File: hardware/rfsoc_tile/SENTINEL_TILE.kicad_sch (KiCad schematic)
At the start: 118 parts, among them J1 SOM CONN A, J10 RX1, J11 RX2, J12 RX3, J13 RX4, J14 RX5, J15 RX6, J16 RX7, J17 RX8, J18 RXCAL, J2 SOM CONN B, J20 TX1, J21 TX2, J22 TX3, J23 TX4, J24 TX5, J25 TX6, J26 TX7, J27 TX8, J28 TXCAL, J3 BACKPLANE, J4 CLOCK, J5 CAL CTRL, J6 PSU LINK, J7 QSFP28, J8 12V IN, T1 1:2, T11 1:2, T12 1:2, T13 1:2, T14 1:2, T15 1:2, T16 1:2, T17 1:2, T18 1:2, T19 1:2, T2 1:2, T3 1:2, T4 1:2, T5 1:2, T6 1:2, T7 1:2, T8 1:2, T9 1:2, U1 THVD1450, U10 LMR33630, U2 THVD1450, U3 THVD1450, U4 THVD1450, U5 THVD1450, U6 THVD1450, U7 THVD1450, U8 THVD1450, U9 THVD1450

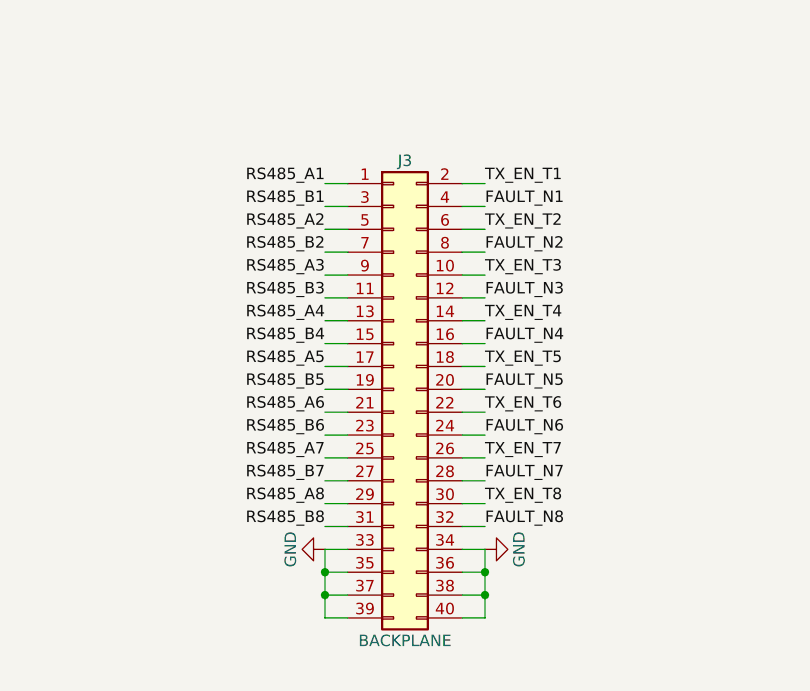
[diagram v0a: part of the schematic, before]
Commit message: Five boards DRC-clean, BOMs, layout engine improvements
- Backplane, clock & timing, calibration network, PSU and feed board layouts now pass
  KiCad DRC with zero errors and zero unconnected items
- T/R module: 0 DRC errors, 6 connections left to route by hand
- Calibration selector redesigned as an SPDT tree (replaces the fine-pitch SP8T)
- PSU: IPC-2221 2.5 mm high-voltage clearance via KiCad custom rules
- Backplane/tile cable re-pinned (slots 1-4 left column, 5-8 right) for routability
- Grouped BOM CSV for every board (hardware/tools/export_bom.sh)
- Router: partial routing, neck-downs at fine-pitch pins, long-axis fan-out,
  NPTH obstacles, pour-net connectivity, domain-aware clearance, rip-up tuning

Co-Authored-By: Claude Opus 5.5 <noreply@anthropic.com>
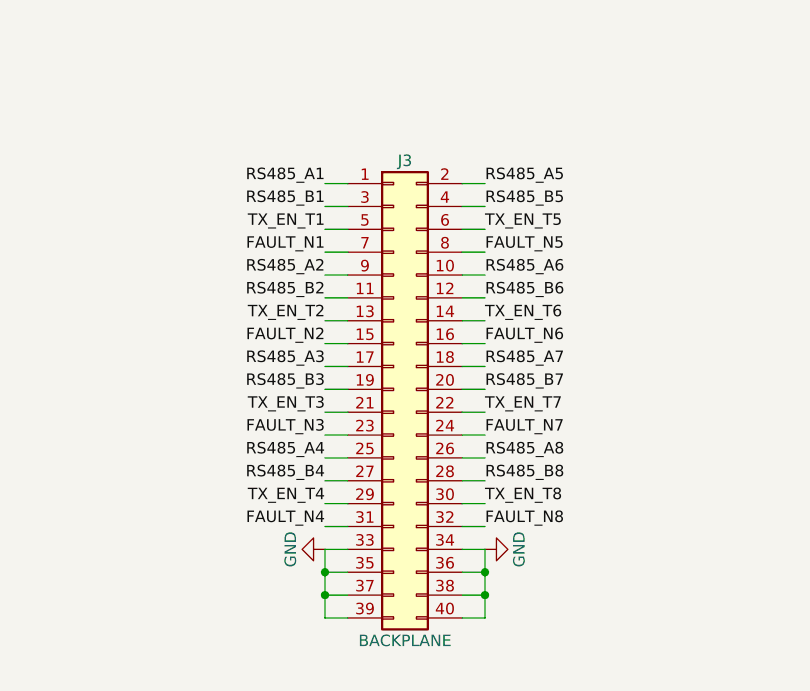
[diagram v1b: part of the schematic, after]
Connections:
- net FAULT_N1: now also J3.7 (Pin_7); no longer J3.4 (Pin_4)
- net FAULT_N2: now also J3.15 (Pin_15); no longer J3.8 (Pin_8)
- net FAULT_N3: now also J3.23 (Pin_23); no longer J3.12 (Pin_12)
- net FAULT_N4: now also J3.31 (Pin_31); no longer J3.16 (Pin_16)
- net FAULT_N5: now also J3.8 (Pin_8); no longer J3.20 (Pin_20)
- net FAULT_N6: now also J3.16 (Pin_16); no longer J3.24 (Pin_24)
- net FAULT_N7: now also J3.24 (Pin_24); no longer J3.28 (Pin_28)
- net RS485_A2: now also J3.9 (Pin_9); no longer J3.5 (Pin_5)
- net RS485_A3: now also J3.17 (Pin_17); no longer J3.9 (Pin_9)
- net RS485_A4: now also J3.25 (Pin_25); no longer J3.13 (Pin_13)
- net RS485_A5: now also J3.2 (Pin_2); no longer J3.17 (Pin_17)
- net RS485_A6: now also J3.10 (Pin_10); no longer J3.21 (Pin_21)
- net RS485_A7: now also J3.18 (Pin_18); no longer J3.25 (Pin_25)
- net RS485_A8: now also J3.26 (Pin_26); no longer J3.29 (Pin_29)
- net RS485_B2: now also J3.11 (Pin_11); no longer J3.7 (Pin_7)
- net RS485_B3: now also J3.19 (Pin_19); no longer J3.11 (Pin_11)
- net RS485_B4: now also J3.27 (Pin_27); no longer J3.15 (Pin_15)
- net RS485_B5: now also J3.4 (Pin_4); no longer J3.19 (Pin_19)
- net RS485_B6: now also J3.12 (Pin_12); no longer J3.23 (Pin_23)
- net RS485_B7: now also J3.20 (Pin_20); no longer J3.27 (Pin_27)
- net RS485_B8: now also J3.28 (Pin_28); no longer J3.31 (Pin_31)
- net TX_EN_T1: now also J3.5 (Pin_5); no longer J3.2 (Pin_2)
- net TX_EN_T2: now also J3.13 (Pin_13); no longer J3.6 (Pin_6)
- net TX_EN_T3: now also J3.21 (Pin_21); no longer J3.10 (Pin_10)
- net TX_EN_T4: now also J3.29 (Pin_29); no longer J3.14 (Pin_14)
- net TX_EN_T5: now also J3.6 (Pin_6); no longer J3.18 (Pin_18)
- net TX_EN_T6: now also J3.14 (Pin_14); no longer J3.22 (Pin_22)
- net TX_EN_T7: now also J3.22 (Pin_22); no longer J3.26 (Pin_26)
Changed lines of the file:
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@@
 		)
 	)
-	(label "TX_EN_T1"
+	(label "RS485_A5"
 		(at 441.96 358.14 0)
 		(fields_autoplaced yes)
@@
 		)
 	)
+	(label "RS485_B5"
+		(at 441.96 360.68 0)
+		(fields_autoplaced yes)
+		(effects
+			(font
+				(size 1.27 1.27)
+			)
+			(justify left bottom)
+		)
+	)
+	(label "TX_EN_T1"
+		(at 424.18 363.22 180)
+		(fields_autoplaced yes)
+		(effects
+			(font
+				(size 1.27 1.27)
+			)
+			(justify right bottom)
+		)
+	)
+	(label "TX_EN_T5"
+		(at 441.96 363.22 0)
+		(fields_autoplaced yes)
+		(effects
+			(font
+				(size 1.27 1.27)
+			)
+			(justify left bottom)
+		)
+	)
 	(label "FAULT_N1"
-		(at 441.96 360.68 0)
+		(at 424.18 365.76 180)
+		(fields_autoplaced yes)
+		(effects
+			(font
+				(size 1.27 1.27)
+			)
+			(justify right bottom)
+		)
+	)
+	(label "FAULT_N5"
+		(at 441.96 365.76 0)
 		(fields_autoplaced yes)
 		(effects
@@
 	)
 	(label "RS485_A2"
-		(at 424.18 363.22 180)
-		(fields_autoplaced yes)
-		(effects
-			(font
-				(size 1.27 1.27)
-			)
-			(justify right bottom)
+		(at 424.18 368.3 180)
+		(fields_autoplaced yes)
+		(effects
+			(font
+				(size 1.27 1.27)
+			)
+			(justify right bottom)
+		)
+	)
+	(label "RS485_A6"
+		(at 441.96 368.3 0)
+		(fields_autoplaced yes)
+		(effects
+			(font
+				(size 1.27 1.27)
+			)
+			(justify left bottom)
+		)
+	)
+	(label "RS485_B2"
+		(at 424.18 370.84 180)
+		(fields_autoplaced yes)
+		(effects
+			(font
+				(size 1.27 1.27)
+			)
+			(justify right bottom)
+		)
+	)
+	(label "RS485_B6"
+		(at 441.96 370.84 0)
+		(fields_autoplaced yes)
+		(effects
+			(font
+				(size 1.27 1.27)
+			)
+			(justify left bottom)
 		)
 	)
 	(label "TX_EN_T2"
-		(at 441.96 363.22 0)
-		(fields_autoplaced yes)
-		(effects
-			(font
-				(size 1.27 1.27)
-			)
-			(justify left bottom)
-		)
-	)
-	(label "RS485_B2"
-		(at 424.18 365.76 180)
-		(fields_autoplaced yes)
-		(effects
-			(font
-				(size 1.27 1.27)
-			)
-			(justify right bottom)
+		(at 424.18 373.38 180)
+		(fields_autoplaced yes)
+		(effects
+			(font
+				(size 1.27 1.27)
+			)
+			(justify right bottom)
+		)
+	)
+	(label "TX_EN_T6"
+		(at 441.96 373.38 0)
+		(fields_autoplaced yes)
+		(effects
+			(font
+				(size 1.27 1.27)
+			)
+			(justify left bottom)
 		)
 	)
 	(label "FAULT_N2"
-		(at 441.96 365.76 0)
+		(at 424.18 375.92 180)
+		(fields_autoplaced yes)
+		(effects
+			(font
+				(size 1.27 1.27)
+			)
+			(justify right bottom)
+		)
+	)
+	(label "FAULT_N6"
+		(at 441.96 375.92 0)
 		(fields_autoplaced yes)
 		(effects
@@
 	)
 	(label "RS485_A3"
-		(at 424.18 368.3 180)
-		(fields_autoplaced yes)
-		(effects
-			(font
-				(size 1.27 1.27)
-			)
-			(justify right bottom)
+		(at 424.18 378.46 180)
+		(fields_autoplaced yes)
+		(effects
+			(font
+				(size 1.27 1.27)
+			)
+			(justify right bottom)
+		)
+	)
+	(label "RS485_A7"
+		(at 441.96 378.46 0)
+		(fields_autoplaced yes)
+		(effects
+			(font
+				(size 1.27 1.27)
+			)
+			(justify left bottom)
+		)
+	)
+	(label "RS485_B3"
+		(at 424.18 381 180)
+		(fields_autoplaced yes)
+		(effects
+			(font
+				(size 1.27 1.27)
+			)
+			(justify right bottom)
+		)
+	)
+	(label "RS485_B7"
+		(at 441.96 381 0)
+		(fields_autoplaced yes)
+		(effects
+			(font
+				(size 1.27 1.27)
+			)
+			(justify left bottom)
 		)
 	)
 	(label "TX_EN_T3"
-		(at 441.96 368.3 0)
-		(fields_autoplaced yes)
-		(effects
-			(font
-				(size 1.27 1.27)
-			)
-			(justify left bottom)
-		)
-	)
-	(label "RS485_B3"
-		(at 424.18 370.84 180)
-		(fields_autoplaced yes)
-		(effects
-			(font
-				(size 1.27 1.27)
-			)
-			(justify right bottom)
+		(at 424.18 383.54 180)
+		(fields_autoplaced yes)
+		(effects
+			(font
+				(size 1.27 1.27)
+			)
+			(justify right bottom)
+		)
+	)
+	(label "TX_EN_T7"
+		(at 441.96 383.54 0)
+		(fields_autoplaced yes)
+		(effects
+			(font
+				(size 1.27 1.27)
+			)
+			(justify left bottom)
 		)
 	)
 	(label "FAULT_N3"
-		(at 441.96 370.84 0)
+		(at 424.18 386.08 180)
+		(fields_autoplaced yes)
+		(effects
+			(font
+				(size 1.27 1.27)
+			)
+			(justify right bottom)
+		)
+	)
+	(label "FAULT_N7"
+		(at 441.96 386.08 0)
 		(fields_autoplaced yes)
 		(effects
@@
 	)
 	(label "RS485_A4"
-		(at 424.18 373.38 180)
-		(fields_autoplaced yes)
-		(effects
-			(font
-				(size 1.27 1.27)
-			)
-			(justify right bottom)
+		(at 424.18 388.62 180)
+		(fields_autoplaced yes)
+		(effects
+			(font
+				(size 1.27 1.27)
+			)
+			(justify right bottom)
+		)
+	)
+	(label "RS485_A8"
+		(at 441.96 388.62 0)
+		(fields_autoplaced yes)
+		(effects
+			(font
+				(size 1.27 1.27)
+			)
+			(justify left bottom)
+		)
+	)
+	(label "RS485_B4"
+		(at 424.18 391.16 180)
+		(fields_autoplaced yes)
+		(effects
+			(font
+				(size 1.27 1.27)
+			)
+			(justify right bottom)
+		)
+	)
+	(label "RS485_B8"
+		(at 441.96 391.16 0)
+		(fields_autoplaced yes)
+		(effects
+			(font
+				(size 1.27 1.27)
+			)
+			(justify left bottom)
 		)
 	)
 	(label "TX_EN_T4"
-		(at 441.96 373.38 0)
-		(fields_autoplaced yes)
-		(effects
-			(font
-				(size 1.27 1.27)
-			)
-			(justify left bottom)
-		)
-	)
-	(label "RS485_B4"
-		(at 424.18 375.92 180)
-		(fields_autoplaced yes)
-		(effects
-			(font
-				(size 1.27 1.27)
-			)
-			(justify right bottom)
-		)
-	)
-	(label "FAULT_N4"
-		(at 441.96 375.92 0)
-		(fields_autoplaced yes)
-		(effects
-			(font
-				(size 1.27 1.27)
-			)
-			(justify left bottom)
-		)
-	)
-	(label "RS485_A5"
-		(at 424.18 378.46 180)
-		(fields_autoplaced yes)
-		(effects
-			(font
-				(size 1.27 1.27)
-			)
-			(justify right bottom)
-		)
-	)
-	(label "TX_EN_T5"
-		(at 441.96 378.46 0)
-		(fields_autoplaced yes)
-		(effects
-			(font
-				(size 1.27 1.27)
-			)
-			(justify left bottom)
-		)
-	)
-	(label "RS485_B5"
-		(at 424.18 381 180)
-		(fields_autoplaced yes)
-		(effects
-			(font
-				(size 1.27 1.27)
-			)
-			(justify right bottom)
-		)
-	)
-	(label "FAULT_N5"
-		(at 441.96 381 0)
-		(fields_autoplaced yes)
-		(effects
-			(font
-				(size 1.27 1.27)
-			)
-			(justify left bottom)
-		)
-	)
-	(label "RS485_A6"
-		(at 424.18 383.54 180)
-		(fields_autoplaced yes)
-		(effects
-			(font
-				(size 1.27 1.27)
-			)
-			(justify right bottom)
-		)
-	)
-	(label "TX_EN_T6"
-		(at 441.96 383.54 0)
-		(fields_autoplaced yes)
-		(effects
-			(font
-				(size 1.27 1.27)
-			)
-			(justify left bottom)
-		)
-	)
-	(label "RS485_B6"
-		(at 424.18 386.08 180)
-		(fields_autoplaced yes)
-		(effects
-			(font
-				(size 1.27 1.27)
-			)
-			(justify right bottom)
-		)
-	)
-	(label "FAULT_N6"
-		(at 441.96 386.08 0)
-		(fields_autoplaced yes)
-		(effects
-			(font
-				(size 1.27 1.27)
-			)
-			(justify left bottom)
-		)
-	)
-	(label "RS485_A7"
-		(at 424.18 388.62 180)
-		(fields_autoplaced yes)
-		(effects
-			(font
-				(size 1.27 1.27)
-			)
-			(justify right bottom)
-		)
-	)
-	(label "TX_EN_T7"
-		(at 441.96 388.62 0)
-		(fields_autoplaced yes)
-		(effects
-			(font
-				(size 1.27 1.27)
-			)
-			(justify left bottom)
-		)
-	)
-	(label "RS485_B7"
-		(at 424.18 391.16 180)
-		(fields_autoplaced yes)
-		(effects
-			(font
-				(size 1.27 1.27)
-			)
-			(justify right bottom)
-		)
-	)
-	(label "FAULT_N7"
-		(at 441.96 391.16 0)
-		(fields_autoplaced yes)
-		(effects
-			(font
-				(size 1.27 1.27)
-			)
-			(justify left bottom)
-		)
-	)
-	(label "RS485_A8"
 		(at 424.18 393.7 180)
 		(fields_autoplaced yes)
@@
 		)
 	)
-	(label "RS485_B8"
+	(label "FAULT_N4"
 		(at 424.18 396.24 180)
 		(fields_autoplaced yes)

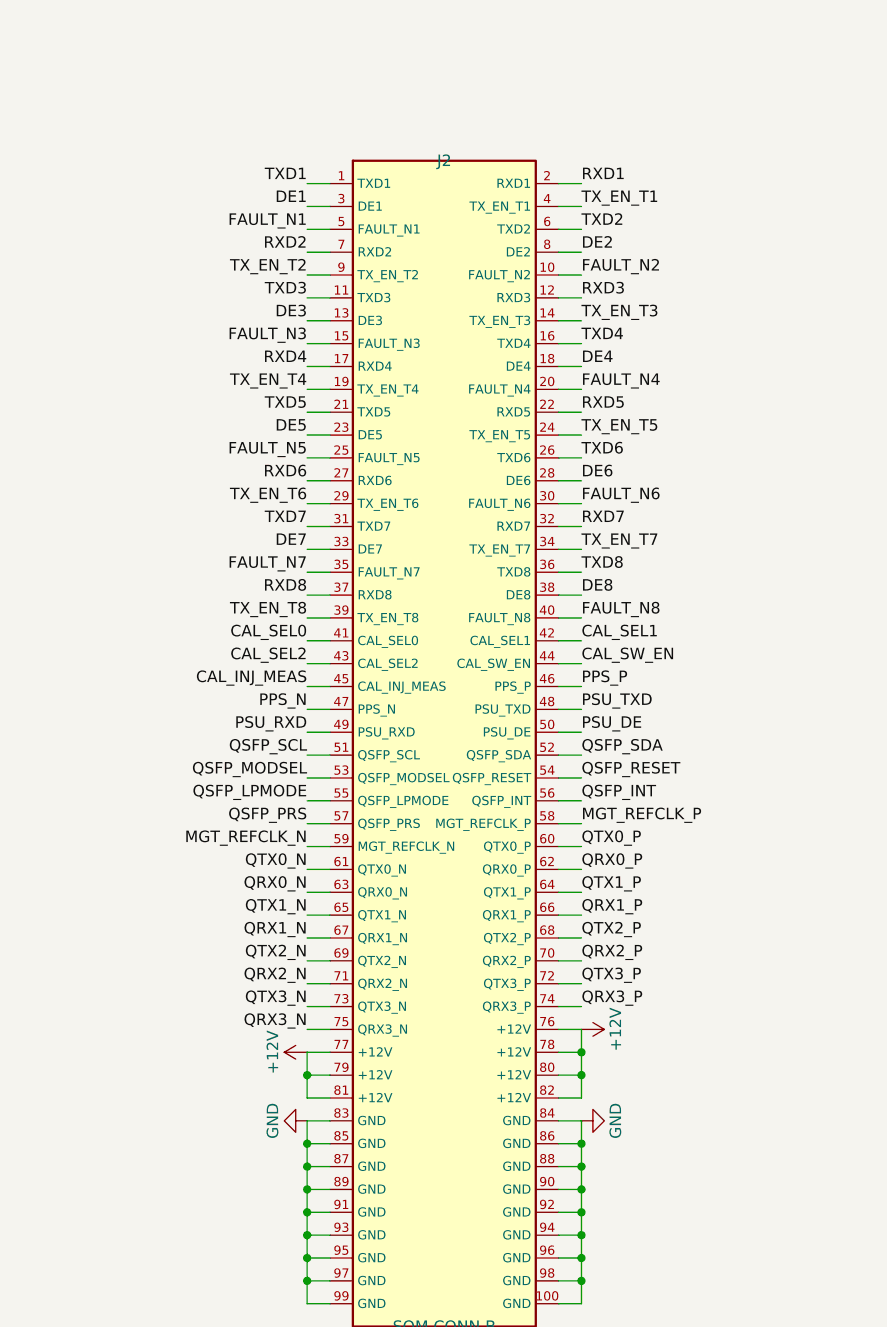
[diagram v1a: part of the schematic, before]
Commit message: RFSoC tile: 320 x 260 mm, routed with EasyEDA Pro, DRC clean
- Board enlarged from 240 x 190 to 320 x 260 mm; SOM connector B pins
  grouped by row toward their destinations (RS-485 / control side).
- Routing done by the EasyEDA Pro autorouter (Top / In2 / Bottom, In1 kept
  as solid GND) and imported back into KiCad: 0 DRC errors, 0 unrouted.
- tools/import_easyeda.py replays easyeda_routes.json onto the KiCad board;
  tools/layer_preview.py draws copper previews from any finished board.
- Regenerated gerbers, 3D view, BOM, figures, report and README (6 of 7
  layouts now DRC clean).

Co-Authored-By: Claude Opus 5.5 <noreply@anthropic.com>
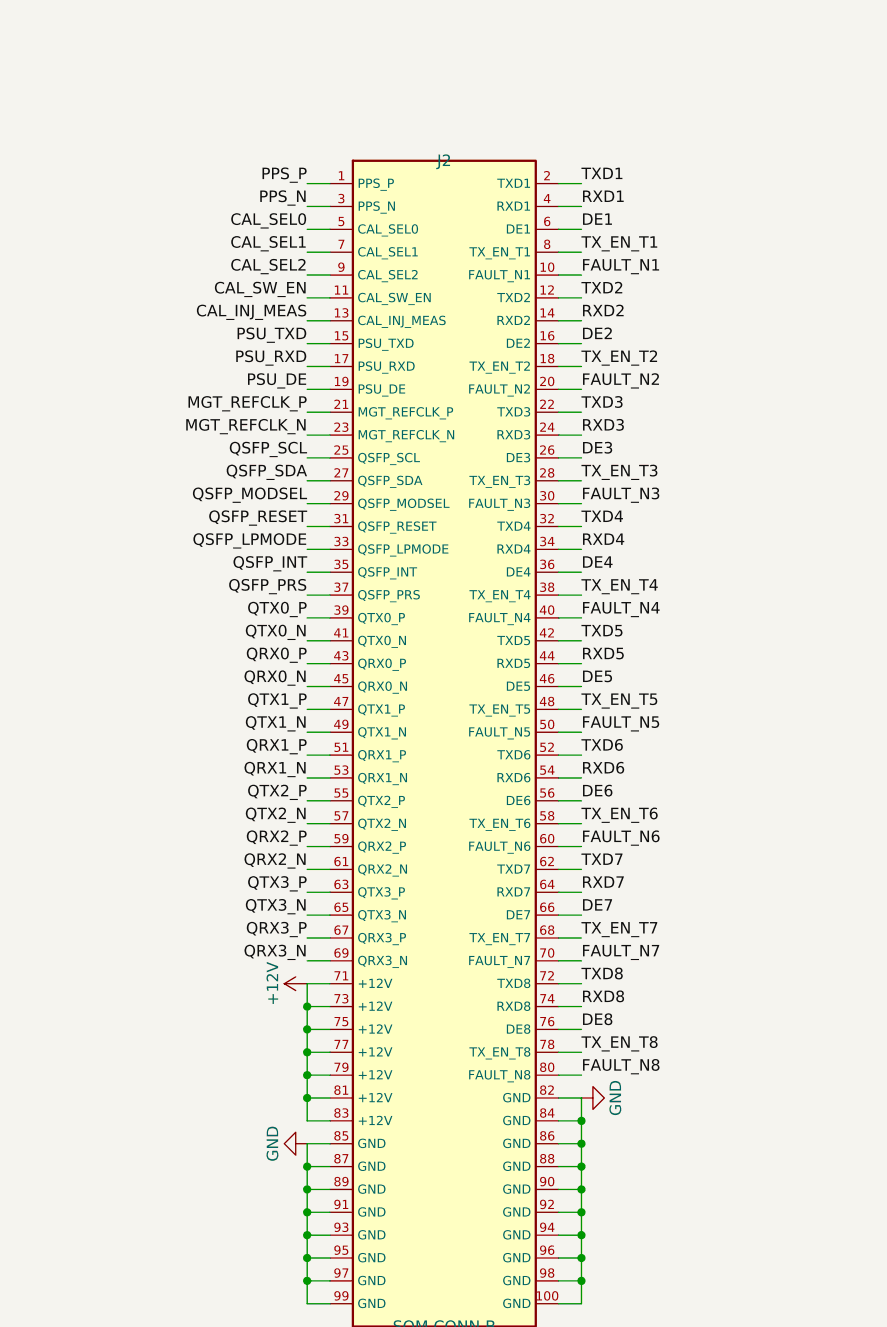
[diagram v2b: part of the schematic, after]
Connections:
- net +12V: now also J2.71 (+12V), J2.73 (+12V), J2.75 (+12V), J2.83 (+12V); no longer J2.76 (+12V), J2.78 (+12V), J2.80 (+12V), J2.82 (+12V)
- net CAL_INJ_MEAS: now also J2.13 (CAL_INJ_MEAS); no longer J2.45 (CAL_INJ_MEAS)
- net CAL_SEL0: now also J2.5 (CAL_SEL0); no longer J2.41 (CAL_SEL0)
- net CAL_SEL1: now also J2.7 (CAL_SEL1); no longer J2.42 (CAL_SEL1)
- net CAL_SEL2: now also J2.9 (CAL_SEL2); no longer J2.43 (CAL_SEL2)
- net CAL_SW_EN: now also J2.11 (CAL_SW_EN); no longer J2.44 (CAL_SW_EN)
- net DE1: now also J2.6 (DE1); no longer J2.3 (DE1)
- net DE2: now also J2.16 (DE2); no longer J2.8 (DE2)
- net DE3: now also J2.26 (DE3); no longer J2.13 (DE3)
- net DE4: now also J2.36 (DE4); no longer J2.18 (DE4)
- net DE5: now also J2.46 (DE5); no longer J2.23 (DE5)
- net DE6: now also J2.56 (DE6); no longer J2.28 (DE6)
- net DE7: now also J2.66 (DE7); no longer J2.33 (DE7)
- net DE8: now also J2.76 (DE8); no longer J2.38 (DE8)
- net FAULT_N1: now also J2.10 (FAULT_N1); no longer J2.5 (FAULT_N1)
- net FAULT_N2: now also J2.20 (FAULT_N2); no longer J2.10 (FAULT_N2)
- net FAULT_N3: now also J2.30 (FAULT_N3); no longer J2.15 (FAULT_N3)
- net FAULT_N4: now also J2.40 (FAULT_N4); no longer J2.20 (FAULT_N4)
- net FAULT_N5: now also J2.50 (FAULT_N5); no longer J2.25 (FAULT_N5)
- net FAULT_N6: now also J2.60 (FAULT_N6); no longer J2.30 (FAULT_N6)
- net FAULT_N7: now also J2.70 (FAULT_N7); no longer J2.35 (FAULT_N7)
- net FAULT_N8: now also J2.80 (FAULT_N8); no longer J2.40 (FAULT_N8)
- net GND: now also J2.82 (GND); no longer J2.83 (GND)
- net MGT_REFCLK_N: now also J2.23 (MGT_REFCLK_N); no longer J2.59 (MGT_REFCLK_N)
- net MGT_REFCLK_P: now also J2.21 (MGT_REFCLK_P); no longer J2.58 (MGT_REFCLK_P)
- net PPS_N: now also J2.3 (PPS_N); no longer J2.47 (PPS_N)
- net PPS_P: now also J2.1 (PPS_P); no longer J2.46 (PPS_P)
- net PSU_DE: now also J2.19 (PSU_DE); no longer J2.50 (PSU_DE)
- net PSU_RXD: now also J2.17 (PSU_RXD); no longer J2.49 (PSU_RXD)
- net PSU_TXD: now also J2.15 (PSU_TXD); no longer J2.48 (PSU_TXD)
- net QRX0_N: now also J2.45 (QRX0_N); no longer J2.63 (QRX0_N)
- net QRX0_P: now also J2.43 (QRX0_P); no longer J2.62 (QRX0_P)
- net QRX1_N: now also J2.53 (QRX1_N); no longer J2.67 (QRX1_N)
- net QRX1_P: now also J2.51 (QRX1_P); no longer J2.66 (QRX1_P)
- net QRX2_N: now also J2.61 (QRX2_N); no longer J2.71 (QRX2_N)
- net QRX2_P: now also J2.59 (QRX2_P); no longer J2.70 (QRX2_P)
- net QRX3_N: now also J2.69 (QRX3_N); no longer J2.75 (QRX3_N)
- net QRX3_P: now also J2.67 (QRX3_P); no longer J2.74 (QRX3_P)
- net QSFP_INT: now also J2.35 (QSFP_INT); no longer J2.56 (QSFP_INT)
- net QSFP_LPMODE: now also J2.33 (QSFP_LPMODE); no longer J2.55 (QSFP_LPMODE)
- net QSFP_MODSEL: now also J2.29 (QSFP_MODSEL); no longer J2.53 (QSFP_MODSEL)
- net QSFP_PRS: now also J2.37 (QSFP_PRS); no longer J2.57 (QSFP_PRS)
- net QSFP_RESET: now also J2.31 (QSFP_RESET); no longer J2.54 (QSFP_RESET)
- net QSFP_SCL: now also J2.25 (QSFP_SCL); no longer J2.51 (QSFP_SCL)
- net QSFP_SDA: now also J2.27 (QSFP_SDA); no longer J2.52 (QSFP_SDA)
- net QTX0_N: now also J2.41 (QTX0_N); no longer J2.61 (QTX0_N)
- net QTX0_P: now also J2.39 (QTX0_P); no longer J2.60 (QTX0_P)
- net QTX1_N: now also J2.49 (QTX1_N); no longer J2.65 (QTX1_N)
- net QTX1_P: now also J2.47 (QTX1_P); no longer J2.64 (QTX1_P)
- net QTX2_N: now also J2.57 (QTX2_N); no longer J2.69 (QTX2_N)
- net QTX2_P: now also J2.55 (QTX2_P); no longer J2.68 (QTX2_P)
- net QTX3_N: now also J2.65 (QTX3_N); no longer J2.73 (QTX3_N)
- net QTX3_P: now also J2.63 (QTX3_P); no longer J2.72 (QTX3_P)
- net RXD1: now also J2.4 (RXD1); no longer J2.2 (RXD1)
- net RXD2: now also J2.14 (RXD2); no longer J2.7 (RXD2)
- net RXD3: now also J2.24 (RXD3); no longer J2.12 (RXD3)
- net RXD4: now also J2.34 (RXD4); no longer J2.17 (RXD4)
- net RXD5: now also J2.44 (RXD5); no longer J2.22 (RXD5)
- net RXD6: now also J2.54 (RXD6); no longer J2.27 (RXD6)
- net RXD7: now also J2.64 (RXD7); no longer J2.32 (RXD7)
- net RXD8: now also J2.74 (RXD8); no longer J2.37 (RXD8)
- net TXD1: now also J2.2 (TXD1); no longer J2.1 (TXD1)
- net TXD2: now also J2.12 (TXD2); no longer J2.6 (TXD2)
- net TXD3: now also J2.22 (TXD3); no longer J2.11 (TXD3)
- net TXD4: now also J2.32 (TXD4); no longer J2.16 (TXD4)
- net TXD5: now also J2.42 (TXD5); no longer J2.21 (TXD5)
- net TXD6: now also J2.52 (TXD6); no longer J2.26 (TXD6)
- net TXD7: now also J2.62 (TXD7); no longer J2.31 (TXD7)
- net TXD8: now also J2.72 (TXD8); no longer J2.36 (TXD8)
- net TX_EN_T1: now also J2.8 (TX_EN_T1); no longer J2.4 (TX_EN_T1)
- net TX_EN_T2: now also J2.18 (TX_EN_T2); no longer J2.9 (TX_EN_T2)
- net TX_EN_T3: now also J2.28 (TX_EN_T3); no longer J2.14 (TX_EN_T3)
- net TX_EN_T4: now also J2.38 (TX_EN_T4); no longer J2.19 (TX_EN_T4)
- net TX_EN_T5: now also J2.48 (TX_EN_T5); no longer J2.24 (TX_EN_T5)
- net TX_EN_T6: now also J2.58 (TX_EN_T6); no longer J2.29 (TX_EN_T6)
- net TX_EN_T7: now also J2.68 (TX_EN_T7); no longer J2.34 (TX_EN_T7)
- net TX_EN_T8: now also J2.78 (TX_EN_T8); no longer J2.39 (TX_EN_T8)
